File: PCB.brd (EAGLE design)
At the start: 55.5 x 68.6 mm, 19 parts, among them IC1 7805TV, IC2 ATMEGA168-PU, IC3 LM35CZ, T1 TIP122

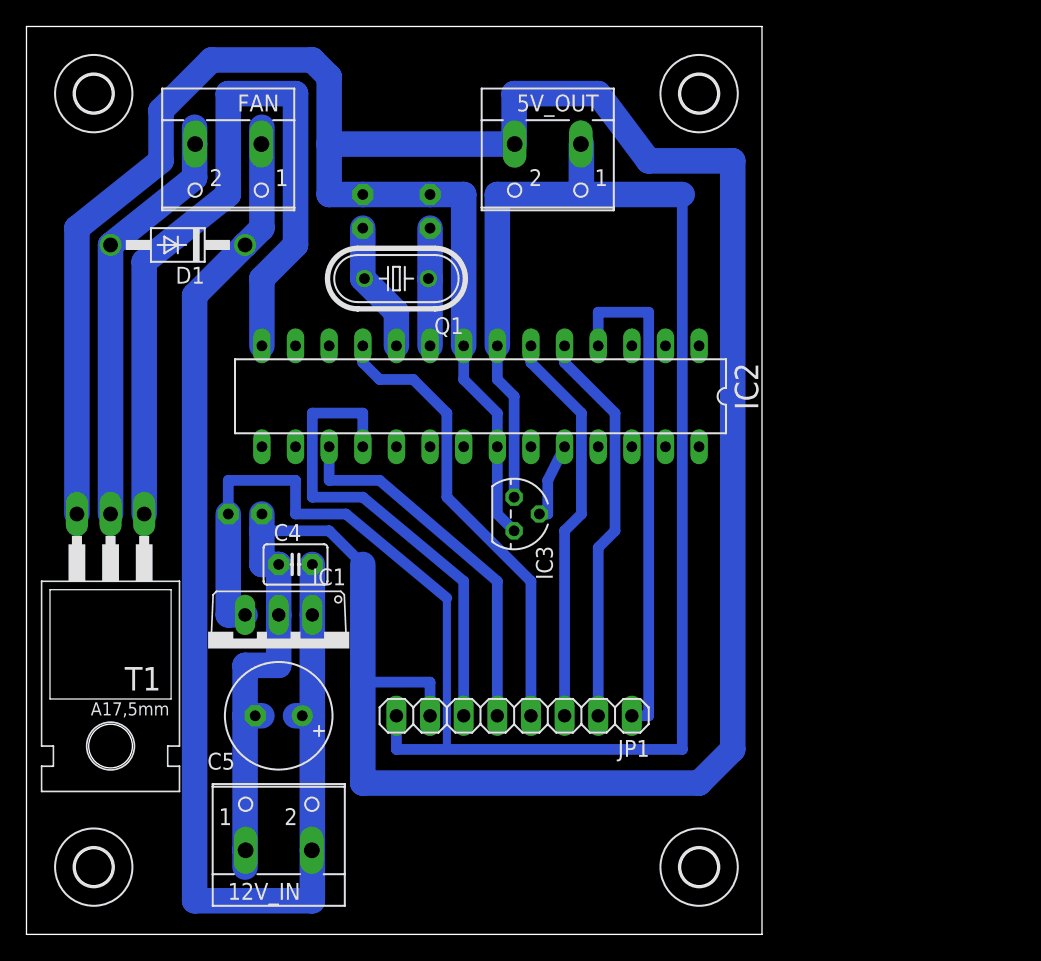
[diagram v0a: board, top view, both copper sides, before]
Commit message: Decoupling capacitor added and resistor
Decoupling capacitor added for driving higher current without noise.
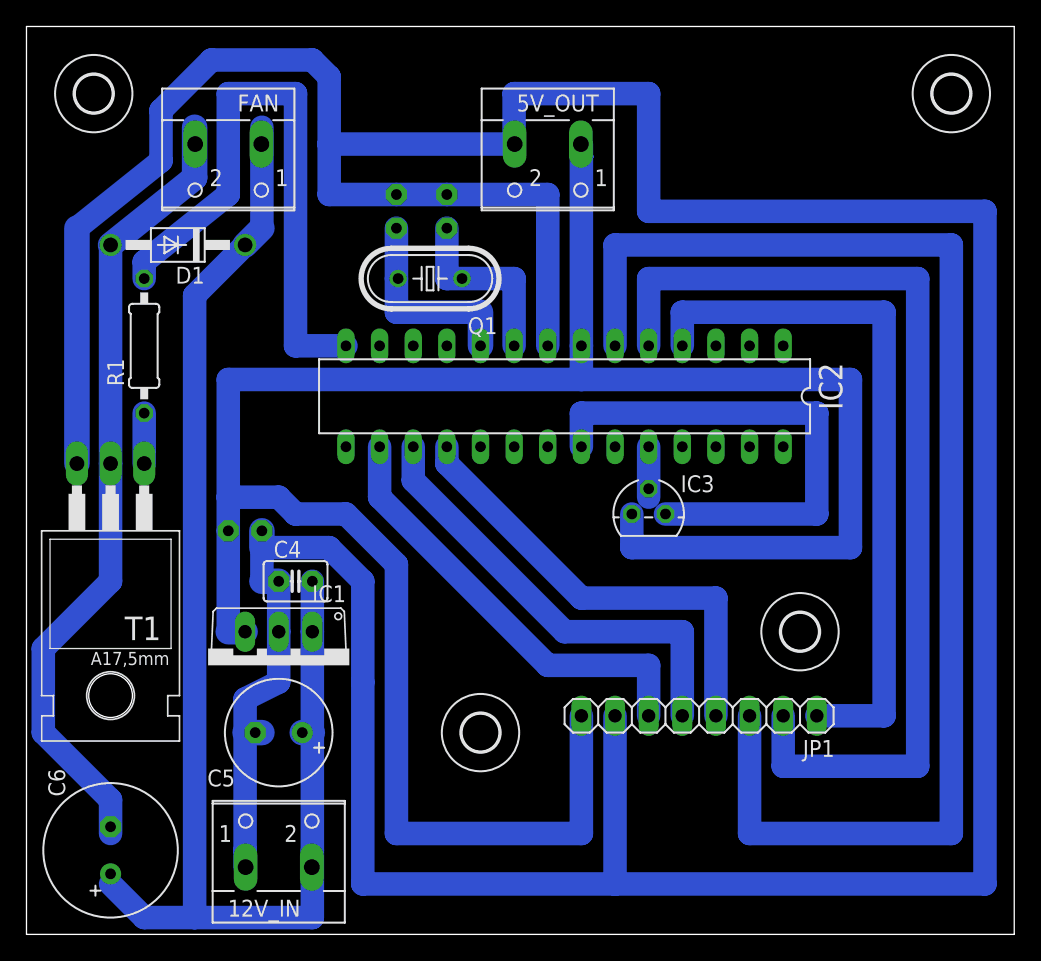
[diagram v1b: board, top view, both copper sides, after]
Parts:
- added C6: 2200uF, resistor:E3,5-10
- added R1: (no value), rcl:0207/10
- moved H4 87.2 mm to (69.8, 63.5)
- moved H3 67.1 mm to (58.4, 22.9)
- moved H2 45.7 mm to (5.08, 63.5)
- moved H1 19.4 mm to (34.3, 15.2)
- moved JP1 14.0 mm to (50.8, 16.5)
- moved IC3 10.2 mm to (47.0, 31.8), turned to 0 degrees
- moved IC2 6.35 mm to (40.6, 40.6)
- moved T1 3.81 mm to (6.35, 29.2)
- moved C2 2.54 mm to (27.9, 54.6)
- moved Q1 2.54 mm to (30.5, 49.5)
- moved C5 1.27 mm to (19.1, 15.2)
- moved 12V_IN 1.27 mm to (19.1, 6.35)
- moved C1 1.27 mm to (31.8, 54.6)
- moved C3 1.27 mm to (16.5, 30.5)
- moved C4 1.27 mm to (20.3, 26.7)
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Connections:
- removed net N$13: D1.A, FAN.2, T1.2
- new net N$18: 12V_IN.2, C4.2, C5.+, C6.+, D1.C, FAN.1, IC1.1
- new net N$2: IC2.16, JP1.6
- net N$11: now also JP1.4; no longer JP1.6
- net N$12: now also R1.2; no longer T1.1
- net N$3: now also C6.-, D1.A, FAN.2, T1.2; no longer 12V_IN.2, C4.2, C5.+, D1.C, FAN.1, IC1.1
- net N$9: now also R1.1, T1.1; no longer IC2.11, JP1.4
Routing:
- net N$18: track 0.00 -> 105.5 mm
- net GND: track 219.9 -> 308.7 mm
- net N$8: track 30.0 -> 101.6 mm
- net N$7: track 30.0 -> 76.2 mm
- net N$3: track 102.5 -> 60.6 mm
- net N$2: track 0.00 -> 33.2 mm
- net N$13: track 32.3 -> 0.00 mm
- net N$9: track 34.7 -> 3.81 mm
- net VCC: track 151.4 -> 176.9 mm
- net N$6: track 38.1 -> 53.3 mm
- net N$12: track 60.0 -> 45.0 mm
- net N$1: track 9.02 -> 15.1 mm
- net N$10: track 28.2 -> 33.9 mm
- net N$4: track 10.1 -> 15.4 mm
- net N$5: track 50.1 -> 47.8 mm
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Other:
- board size 55.5 x 68.6 mm -> 74.6 x 68.6 mm
